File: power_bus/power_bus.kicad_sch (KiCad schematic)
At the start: 28 parts, among them J1 Conn_02x08_Odd_Even, J10 Conn_02x08_Odd_Even, J11 Conn_02x08_Odd_Even, J12 Conn_02x08_Odd_Even, J13 Conn_02x08_Odd_Even, J14 Conn_02x08_Odd_Even, J15 Conn_02x08_Odd_Even, J16 Conn_02x08_Odd_Even, J17 Conn_02x08_Odd_Even, J18 Conn_02x08_Odd_Even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

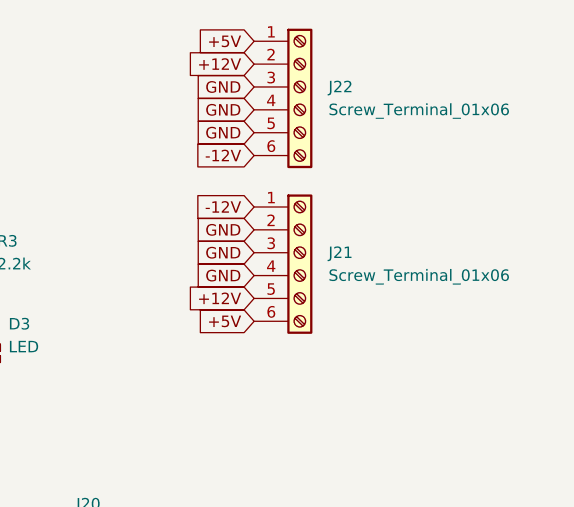
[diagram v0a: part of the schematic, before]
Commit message: Added mega_12v_pwr
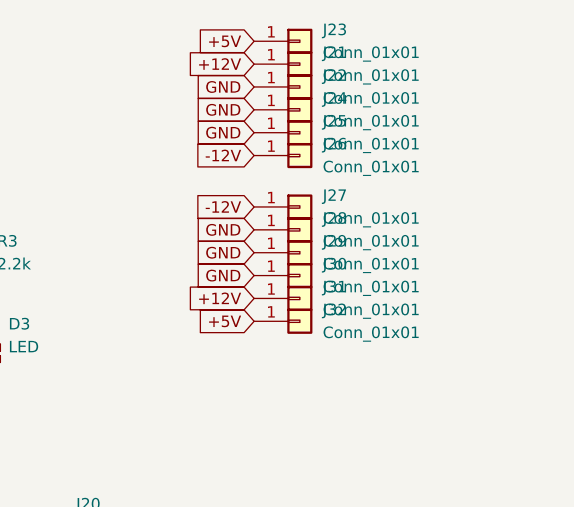
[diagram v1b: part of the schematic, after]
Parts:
- removed J21, J22: Screw_Terminal_01x06, TerminalBlock_Phoenix:TerminalBlock_Phoenix_MKDS-1,5-6-5.08_1x06_P5.08mm_Horizontal, symbol Connector:Screw_Terminal_01x06
- added J21, J22, J23, J24, J25, J26, J27, J28, J29, J30, J31, J32: Conn_01x01, AlexCustom:SPADE, symbol Connector_Generic:Conn_01x01
- R1, R2, R3: footprint PCM_4ms_Resistor:R_Axial_DIN0207_L6.3mm_D2.5mm_P7.62mm_Horizontal -> Resistor_THT:R_Axial_DIN0207_L6.3mm_D2.5mm_P7.62mm_Horizontal
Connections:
- net +12V: now also J21.1 (Pin_1), J31.1 (Pin_1)
- net +5V: now also J23.1 (Pin_1), J32.1 (Pin_1)
- net -12V: now also J26.1 (Pin_1), J27.1 (Pin_1)
- net GND: now also J22.1 (Pin_1), J24.1 (Pin_1), J25.1 (Pin_1), J28.1 (Pin_1), J29.1 (Pin_1), J30.1 (Pin_1)

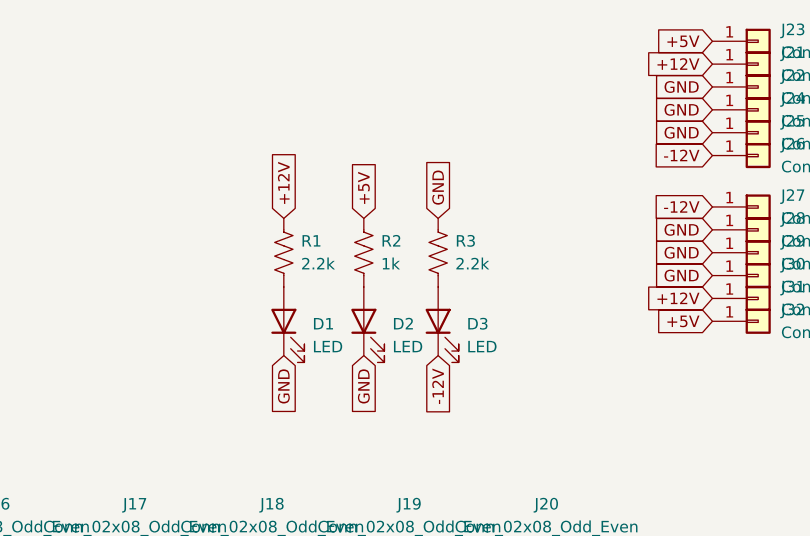
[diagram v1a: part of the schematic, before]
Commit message: Updated resistor values
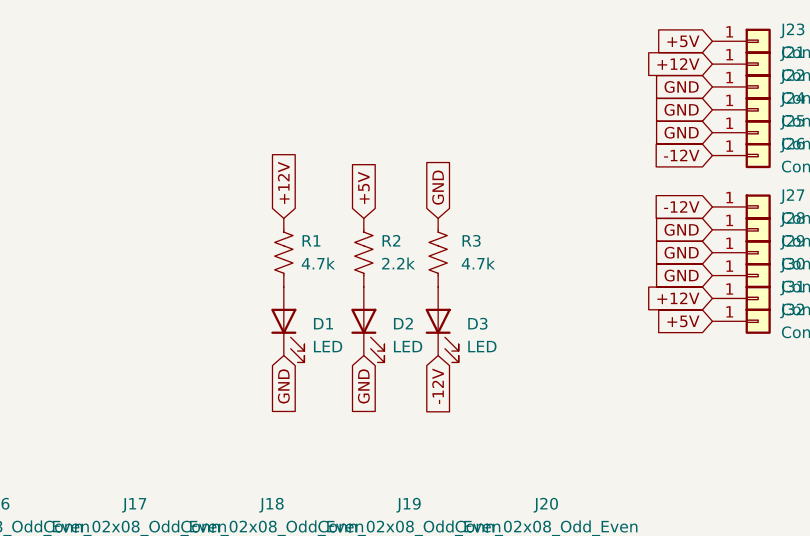
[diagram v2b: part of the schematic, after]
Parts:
- R1, R3: value 2.2k -> 4.7k
- R2: value 1k -> 2.2k
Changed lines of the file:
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@@
       (effects (font (size 1.27 1.27)) (justify left))
     )
-    (property "Value" "1k" (at 327.66 115.57 0)
+    (property "Value" "2.2k" (at 327.66 115.57 0)
       (effects (font (size 1.27 1.27)) (justify left))
     )
@@
   (symbol (lib_id "Device:R_US") (at 334.01 114.3 0) (unit 1)
     (in_bom yes) (on_board yes) (dnp no) (fields_autoplaced)
-    (property "Reference" "R3" (at 335.915 113.03 0)
+    (property "Reference" "R3" (at 336.55 113.03 0)
       (effects (font (size 1.27 1.27)) (justify left))
     )
-    (property "Value" "2.2k" (at 335.915 115.57 0)
+    (property "Value" "4.7k" (at 336.55 115.57 0)
       (effects (font (size 1.27 1.27)) (justify left))
     )
@@
       (effects (font (size 1.27 1.27)) (justify left))
     )
-    (property "Value" "2.2k" (at 318.77 115.57 0)
+    (property "Value" "4.7k" (at 318.77 115.57 0)
       (effects (font (size 1.27 1.27)) (justify left))
     )

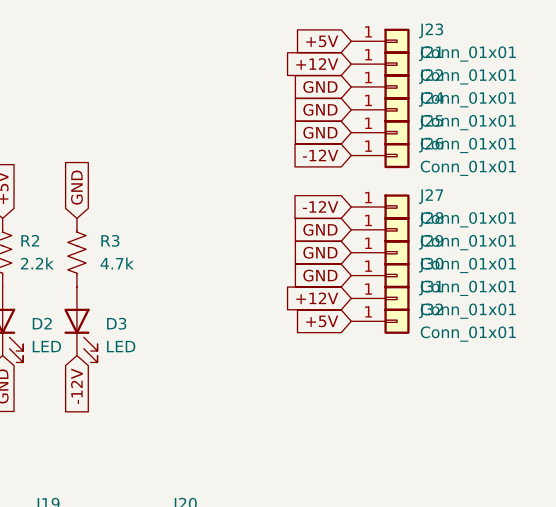
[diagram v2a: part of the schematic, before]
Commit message: Moved spade connectors
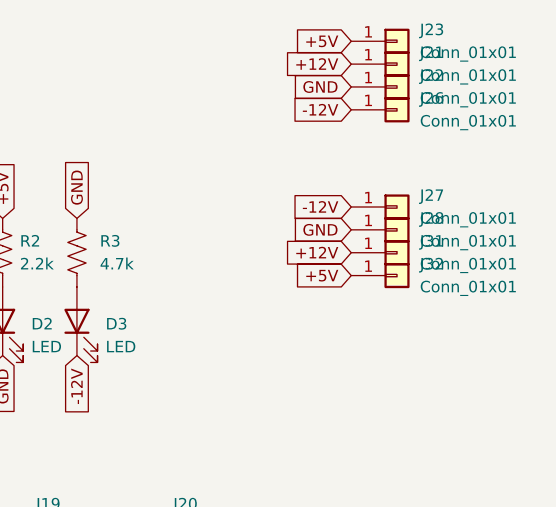
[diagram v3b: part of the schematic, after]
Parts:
- removed J24, J25, J29, J30: Conn_01x01, AlexCustom:SPADE, symbol Connector_Generic:Conn_01x01
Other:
- moved on the sheet: J26, J31, J32
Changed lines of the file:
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@@
-    )
-  )
-  (global_label "GND" (shape input) (at 364.49 100.965 180) (fields_autoplaced)
-    (effects (font (size 1.27 1.27)) (justify right))
-    (property "Intersheetrefs" "${INTERSHEET_REFS}" (at 357.6343 100.965 0)
-      (effects (font (size 1.27 1.27)) (justify right) hide)
     )
   )
@@
     )
   )
-  (global_label "GND" (shape input) (at 364.49 116.84 180) (fields_autoplaced)
-    (effects (font (size 1.27 1.27)) (justify right))
-    (property "Intersheetrefs" "${INTERSHEET_REFS}" (at 357.6343 116.84 0)
-      (effects (font (size 1.27 1.27)) (justify right) hide)
-    )
-  )
-  (global_label "GND" (shape input) (at 364.49 114.3 180) (fields_autoplaced)
-    (effects (font (size 1.27 1.27)) (justify right))
-    (property "Intersheetrefs" "${INTERSHEET_REFS}" (at 357.6343 114.3 0)
-      (effects (font (size 1.27 1.27)) (justify right) hide)
-    )
-  )
   (global_label "CV" (shape input) (at 355.6 163.83 0) (fields_autoplaced)
     (effects (font (size 1.27 1.27)) (justify left))
@@
     )
   )
-  (global_label "+12V" (shape input) (at 364.49 119.38 180) (fields_autoplaced)
+  (global_label "+12V" (shape input) (at 364.49 114.3 180) (fields_autoplaced)
     (effects (font (size 1.27 1.27)) (justify right))
-    (property "Intersheetrefs" "${INTERSHEET_REFS}" (at 356.4248 119.38 0)
+    (property "Intersheetrefs" "${INTERSHEET_REFS}" (at 356.4248 114.3 0)
       (effects (font (size 1.27 1.27)) (justify right) hide)
     )
@@
     )
   )
-  (global_label "+5V" (shape input) (at 364.49 121.92 180) (fields_autoplaced)
+  (global_label "+5V" (shape input) (at 364.49 116.84 180) (fields_autoplaced)
     (effects (font (size 1.27 1.27)) (justify right))
-    (property "Intersheetrefs" "${INTERSHEET_REFS}" (at 357.6343 121.92 0)
+    (property "Intersheetrefs" "${INTERSHEET_REFS}" (at 357.6343 116.84 0)
       (effects (font (size 1.27 1.27)) (justify right) hide)
     )
@@
     )
   )
-  (global_label "-12V" (shape input) (at 364.49 103.505 180) (fields_autoplaced)
+  (global_label "-12V" (shape input) (at 364.49 98.425 180) (fields_autoplaced)
     (effects (font (size 1.27 1.27)) (justify right))
-    (property "Intersheetrefs" "${INTERSHEET_REFS}" (at 356.4248 103.505 0)
+    (property "Intersheetrefs" "${INTERSHEET_REFS}" (at 356.4248 98.425 0)
       (effects (font (size 1.27 1.27)) (justify right) hide)
     )
@@
     )
   )
-  (global_label "GND" (shape input) (at 364.49 98.425 180) (fields_autoplaced)
-    (effects (font (size 1.27 1.27)) (justify right))
-    (property "Intersheetrefs" "${INTERSHEET_REFS}" (at 357.6343 98.425 0)
-      (effects (font (size 1.27 1.27)) (justify right) hide)
-    )
-  )
   (symbol (lib_id "Connector_Generic:Conn_02x08_Odd_Even") (at 252.73 156.21 0) (unit 1)
     (in_bom yes) (on_board yes) (dnp no) (fields_autoplaced)
@@
     )
   )
-  (symbol (lib_id "Connector_Generic:Conn_01x01") (at 369.57 121.92 0) (unit 1)
-    (in_bom yes) (on_board yes) (dnp no) (fields_autoplaced)
-    (property "Reference" "J32" (at 372.11 120.65 0)
-      (effects (font (size 1.27 1.27)) (justify left))
-    )
-    (property "Value" "Conn_01x01" (at 372.11 123.19 0)
-      (effects (font (size 1.27 1.27)) (justify left))
-    )
-    (property "Footprint" "AlexCustom:SPADE" (at 369.57 121.92 0)
-      (effects (font (size 1.27 1.27)) hide)
-    )
-    (property "Datasheet" "~" (at 369.57 121.92 0)
+  (symbol (lib_id "Connector_Generic:Conn_01x01") (at 369.57 116.84 0) (unit 1)
+    (in_bom yes) (on_board yes) (dnp no) (fields_autoplaced)
+    (property "Reference" "J32" (at 372.11 115.57 0)
+      (effects (font (size 1.27 1.27)) (justify left))
+    )
+    (property "Value" "Conn_01x01" (at 372.11 118.11 0)
+      (effects (font (size 1.27 1.27)) (justify left))
+    )
+    (property "Footprint" "AlexCustom:SPADE" (at 369.57 116.84 0)
+      (effects (font (size 1.27 1.27)) hide)
+    )
+    (property "Datasheet" "~" (at 369.57 116.84 0)
       (effects (font (size 1.27 1.27)) hide)
     )
@@
     )
   )
-  (symbol (lib_id "Connector_Generic:Conn_01x01") (at 369.57 103.505 0) (unit 1)
-    (in_bom yes) (on_board yes) (dnp no) (fields_autoplaced)
-    (property "Reference" "J26" (at 372.11 102.235 0)
-      (effects (font (size 1.27 1.27)) (justify left))
-    )
-    (property "Value" "Conn_01x01" (at 372.11 104.775 0)
-      (effects (font (size 1.27 1.27)) (justify left))
-    )
-    (property "Footprint" "AlexCustom:SPADE" (at 369.57 103.505 0)
-      (effects (font (size 1.27 1.27)) hide)
-    )
-    (property "Datasheet" "~" (at 369.57 103.505 0)
+  (symbol (lib_id "Connector_Generic:Conn_01x01") (at 369.57 98.425 0) (unit 1)
+    (in_bom yes) (on_board yes) (dnp no) (fields_autoplaced)
+    (property "Reference" "J26" (at 372.11 97.155 0)
+      (effects (font (size 1.27 1.27)) (justify left))
+    )
+    (property "Value" "Conn_01x01" (at 372.11 99.695 0)
+      (effects (font (size 1.27 1.27)) (justify left))
+    )
+    (property "Footprint" "AlexCustom:SPADE" (at 369.57 98.425 0)
+      (effects (font (size 1.27 1.27)) hide)
+    )
+    (property "Datasheet" "~" (at 369.57 98.425 0)
       (effects (font (size 1.27 1.27)) hide)
     )
@@
         (path "/0ae39bc7-279d-43f1-89d9-43c7f2812868"
           (reference "J9") (unit 1)
-        )
-      )
-    )
-  )
-  (symbol (lib_id "Connector_Generic:Conn_01x01") (at 369.57 114.3 0) (unit 1)
-    (in_bom yes) (on_board yes) (dnp no) (fields_autoplaced)
-    (property "Reference" "J29" (at 372.11 113.03 0)
-      (effects (font (size 1.27 1.27)) (justify left))
-    )
-    (property "Value" "Conn_01x01" (at 372.11 115.57 0)
-      (effects (font (size 1.27 1.27)) (justify left))
-    )
-    (property "Footprint" "AlexCustom:SPADE" (at 369.57 114.3 0)
-      (effects (font (size 1.27 1.27)) hide)
-    )
-    (property "Datasheet" "~" (at 369.57 114.3 0)
-      (effects (font (size 1.27 1.27)) hide)
-    )
-    (pin "1")
-    (instances
-      (project "power_bus"
-        (path "/0ae39bc7-279d-43f1-89d9-43c7f2812868"
-          (reference "J29") (unit 1)
-        )
-      )
-    )
-  )
-  (symbol (lib_id "Connector_Generic:Conn_01x01") (at 369.57 100.965 0) (unit 1)
-    (in_bom yes) (on_board yes) (dnp no) (fields_autoplaced)
-    (property "Reference" "J25" (at 372.11 99.695 0)
-      (effects (font (size 1.27 1.27)) (justify left))
-    )
-    (property "Value" "Conn_01x01" (at 372.11 102.235 0)
-      (effects (font (size 1.27 1.27)) (justify left))
-    )
-    (property "Footprint" "AlexCustom:SPADE" (at 369.57 100.965 0)
-      (effects (font (size 1.27 1.27)) hide)
-    )
-    (property "Datasheet" "~" (at 369.57 100.965 0)
-      (effects (font (size 1.27 1.27)) hide)
-    )
-    (pin "1")
-    (instances
-      (project "power_bus"
-        (path "/0ae39bc7-279d-43f1-89d9-43c7f2812868"
-          (reference "J25") (unit 1)
         )
       )
@@
     )
   )
-  (symbol (lib_id "Connector_Generic:Conn_01x01") (at 369.57 98.425 0) (unit 1)
-    (in_bom yes) (on_board yes) (dnp no) (fields_autoplaced)
-    (property "Reference" "J24" (at 372.11 97.155 0)
-      (effects (font (size 1.27 1.27)) (justify left))
-    )
-    (property "Value" "Conn_01x01" (at 372.11 99.695 0)
-      (effects (font (size 1.27 1.27)) (justify left))
-    )
-    (property "Footprint" "AlexCustom:SPADE" (at 369.57 98.425 0)
-      (effects (font (size 1.27 1.27)) hide)
-    )
-    (property "Datasheet" "~" (at 369.57 98.425 0)
-      (effects (font (size 1.27 1.27)) hide)
-    )
-    (pin "1")
-    (instances
-      (project "power_bus"
-        (path "/0ae39bc7-279d-43f1-89d9-43c7f2812868"
-          (reference "J24") (unit 1)
-        )
-      )
-    )
-  )
-  (symbol (lib_id "Connector_Generic:Conn_01x01") (at 369.57 116.84 0) (unit 1)
-    (in_bom yes) (on_board yes) (dnp no) (fields_autoplaced)
-    (property "Reference" "J30" (at 372.11 115.57 0)
-      (effects (font (size 1.27 1.27)) (justify left))
-    )
-    (property "Value" "Conn_01x01" (at 372.11 118.11 0)
-      (effects (font (size 1.27 1.27)) (justify left))
-    )
-    (property "Footprint" "AlexCustom:SPADE" (at 369.57 116.84 0)
-      (effects (font (size 1.27 1.27)) hide)
-    )
-    (property "Datasheet" "~" (at 369.57 116.84 0)
-      (effects (font (size 1.27 1.27)) hide)
-    )
-    (pin "1")
-    (instances
-      (project "power_bus"
-        (path "/0ae39bc7-279d-43f1-89d9-43c7f2812868"
-          (reference "J30") (unit 1)
-        )
-      )
-    )
-  )
   (symbol (lib_id "Connector_Generic:Conn_02x08_Odd_Even") (at 161.29 156.21 0) (unit 1)
     (in_bom yes) (on_board yes) (dnp no) (fields_autoplaced)
@@
     )
   )
-  (symbol (lib_id "Connector_Generic:Conn_01x01") (at 369.57 119.38 0) (unit 1)
-    (in_bom yes) (on_board yes) (dnp no) (fields_autoplaced)
-    (property "Reference" "J31" (at 372.11 118.11 0)
-      (effects (font (size 1.27 1.27)) (justify left))
-    )
-    (property "Value" "Conn_01x01" (at 372.11 120.65 0)
-      (effects (font (size 1.27 1.27)) (justify left))
-    )
-    (property "Footprint" "AlexCustom:SPADE" (at 369.57 119.38 0)
-      (effects (font (size 1.27 1.27)) hide)
-    )
-    (property "Datasheet" "~" (at 369.57 119.38 0)
-      (effects (font (size 1.27 1.27)) hide)
-    )
+  (symbol (lib_id "Connector_Generic:Conn_01x01") (at 369.57 114.3 0) (unit 1)
+    (in_bom yes) (on_board yes) (dnp no) (fields_autoplaced)
+    (property "Reference" "J31" (at 372.11 113.03 0)
+      (effects (font (size 1.27 1.27)) (justify left))
+    )
+    (property "Value" "Conn_01x01" (at 372.11 115.57 0)
+      (effects (font (size 1.27 1.27)) (justify left))
+    )
+    (property "Footprint" "AlexCustom:SPADE" (at 369.57 114.3 0)
+      (effects (font (size 1.27 1.27)) hide)
+    )
+    (property "Datasheet" "~" (at 369.57 114.3 0)
+      (effects (font (size 1.27 1.27)) hide)
+    )
